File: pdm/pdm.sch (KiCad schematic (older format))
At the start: 30 parts, among them J1 Conn_01x04_Male, J2 Conn_01x04_Female, J3 Conn_01x02_Male, J4 Conn_01x12_Male, U1 SN65HVD233, U2 LM2937xS, Y1 32Mhz

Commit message: polished layout
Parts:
- gave numbers to parts that had none: 1
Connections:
- net act1: now also U3.13 (PA7); no longer U3.14 (PB0)
- net act2: now also U3.15 (PB1); no longer U3.26 (PB3)
- net act3: now also U3.19 (PA9); no longer U3.13 (PA7)
- net act4: now also U3.26 (PB3); no longer U3.20 (PA10)
- net act5: now also U3.27 (PB4); no longer U3.19 (PA9)
- net fuse1: now also U3.12 (PA6); no longer U3.25 (PA15)
- net fuse2: now also U3.14 (PB0); no longer U3.15 (PB1)
- net fuse3: now also U3.18 (PA8); no longer U3.12 (PA6)
- net fuse4: now also U3.25 (PA15); no longer U3.27 (PB4)
- net fuse5: now also U3.28 (PB5); no longer U3.18 (PA8)
- net sense1: now also U3.10 (PA4); no longer U3.9 (PA3)
- net sense2: now also U3.9 (PA3); no longer U3.10 (PA4)
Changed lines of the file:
@@
 	1    0    0    -1
 $EndComp
-Text Label 5150 5400 0    50   ~ 0
+Text Label 5100 5400 0    50   ~ 0
 OSC_P
-Text Label 5150 5300 0    50   ~ 0
+Text Label 5100 5300 0    50   ~ 0
 OSC_N
 Wire Wire Line
-	5750 5400 5150 5400
-Wire Wire Line
-	5750 5300 5150 5300
+	5750 5400 5100 5400
+Wire Wire Line
+	5750 5300 5100 5300
 Wire Wire Line
 	5150 4700 5750 4700
@@
 Wire Wire Line
 	5450 9050 5700 9050
-Text Label 5100 5900 0    50   ~ 0
+Text Label 7400 6200 2    50   ~ 0
 fuse4
 Wire Wire Line
-	6750 5700 7400 5700
-Text Label 7400 5700 2    50   ~ 0
+	5750 5800 5100 5800
+Text Label 5100 5800 0    50   ~ 0
 act4
 Wire Wire Line
-	5750 5900 5100 5900
+	6750 6200 7400 6200
 Wire Wire Line
 	6150 6450 6250 6450
@@
 	2800 1850 3100 1850
 Wire Wire Line
-	6750 6200 7400 6200
-Text Label 7400 6200 2    50   ~ 0
+	6750 5300 7400 5300
+Text Label 7400 5300 2    50   ~ 0
 fuse1
-Wire Wire Line
-	6750 5400 7400 5400
-Text Label 7400 5400 2    50   ~ 0
-act3
-Text Label 7400 5300 2    50   ~ 0
-fuse3
-Wire Wire Line
-	6750 5300 7400 5300
-Text Label 7400 5600 2    50   ~ 0
-act5
-Text Label 7400 5500 2    50   ~ 0
-fuse5
-Wire Wire Line
-	6750 5500 7400 5500
-Wire Wire Line
-	6750 5600 7400 5600
 $Comp
 L pdm-rescue:TestPoint_Probe-Connector TP?
@@
 Wire Wire Line
 	3200 7100 3200 7200
+Text Label 7400 5400 2    50   ~ 0
+act1
+Wire Wire Line
+	6750 5400 7400 5400
 Text Label 5100 5600 0    50   ~ 0
-act1
+fuse2
 Wire Wire Line
 	5750 5600 5100 5600
+Wire Wire Line
+	5750 5700 5100 5700
 Text Label 5100 5700 0    50   ~ 0
-fuse2
-Wire Wire Line
-	5750 5700 5100 5700
-Wire Wire Line
-	5750 5800 5100 5800
-Text Label 5100 5800 0    50   ~ 0
 act2
 $Comp
@@
 	2850 2050 2650 2050
 $Comp
-L MCU_ST_STM32L4:STM32L432KCUx U?
+L MCU_ST_STM32L4:STM32L432KCUx U3
 U 1 1 60CFF808
 P 6250 5400
-F 0 "U?" H 6250 6481 50  0000 C CNN
+F 0 "U3" H 6250 6481 50  0000 C CNN
 F 1 "STM32L432KCUx" H 6250 6390 50  0000 C CNN
 F 2 "Package_DFN_QFN:QFN-32-1EP_5x5mm_P0.5mm_EP3.45x3.45mm" H 5850 4500 50  0001 R CNN
@@
 Wire Wire Line
 	6750 4700 7400 4700
-Text Label 7400 5000 2    50   ~ 0
+Text Label 7400 5100 2    50   ~ 0
 sense1
 Wire Wire Line
-	6750 5000 7400 5000
+	6750 5100 7400 5100
 Wire Wire Line
 	6750 4900 7400 4900
 Text Label 7400 4900 2    50   ~ 0
 sense3
-Text Label 7400 5100 2    50   ~ 0
+Text Label 7400 5000 2    50   ~ 0
 sense2
 Wire Wire Line
-	6750 5100 7400 5100
+	6750 5000 7400 5000
 Text Label 7400 5200 2    50   ~ 0
 DAC2
@@
 Wire Wire Line
 	6350 4450 6350 4500
+Wire Wire Line
+	5750 5900 5100 5900
+Wire Wire Line
+	5750 6000 5100 6000
+Text Label 5100 6000 0    50   ~ 0
+fuse5
+Text Label 5100 5900 0    50   ~ 0
+act5
+Wire Wire Line
+	6750 5500 7400 5500
+Text Label 7400 5500 2    50   ~ 0
+fuse3
+Text Label 7400 5600 2    50   ~ 0
+act3
+Wire Wire Line
+	6750 5600 7400 5600
 $EndSCHEMATC

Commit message: general changes
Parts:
- removed J2: Conn_01x04_Female, Connector_PinHeader_2.54mm:PinHeader_1x04_P2.54mm_Vertical, symbol Connector:Conn_01x04_Female
- added H5: MountingHole, pdm_v2:pepe-v2, symbol Mechanical:MountingHole
- added H6: MountingHole, pdm_v2:uwam-logo, symbol Mechanical:MountingHole
- added H7: MountingHole, pdm_v2:checklist, symbol Mechanical:MountingHole
- added H8: MountingHole, pdm_v2:meme-qr, symbol Mechanical:MountingHole
- added J2: Conn_01x14_Female, Connector_PinSocket_1.27mm:PinSocket_2x07_P1.27mm_Vertical_SMD, symbol Connector:Conn_01x14_Female
- C10: value 1uF -> 0.1pF; Digi-Key_PN 1276-1859-2-ND -> (none)
- U3: footprint Package_DFN_QFN:QFN-32-1EP_5x5mm_P0.5mm_EP3.45x3.45mm -> Package_DFN_QFN:QFN-32-1EP_5x5mm_P0.5mm_EP3.45x3.45mm_ThermalVias
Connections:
- net +3V3: now also J2.3 (Pin_3); no longer C10.1
- net GND: now also J2.5 (Pin_5), J2.7 (Pin_7)
- net NRST: now also C10.1, J2.12 (Pin_12)
- net SWCLK: now also J2.6 (Pin_6)
- net SWDIO: now also J2.4 (Pin_4)
- new net GNDDetect: J2.11 (Pin_11)
- new net JCLK: J2.9 (Pin_9)
- new net SWO: J2.8 (Pin_8)
- new net T_JTDI: J2.10 (Pin_10)
- new net VCP_RX: J2.13 (Pin_13)
- new net VCP_TX: J2.14 (Pin_14)
- no-connect marks 0 -> 11

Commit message: Initial commit
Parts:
- removed J2: Conn_01x14_Female, Connector_PinSocket_1.27mm:PinSocket_2x07_P1.27mm_Vertical_SMD, symbol Connector:Conn_01x14_Female
- added TP20: TestPoint_Probe, TestPoint:TestPoint_THTPad_1.0x1.0mm_Drill0.5mm, symbol pdm-rescue:TestPoint_Probe-Connector
- added U9: STLINK_V3, pdm_v2:STM32_Programmer, symbol Project_Libraries:STLINK_V3
- C1, C4, C6, C7: Mouser PN 603-CC0805MRX77BB104 -> 80-C0603C104K3RC7013
- C10: Mouser PN (none) -> 791-RF18N0R1B500CT
- C2, C3: Mouser PN 603-CC805JRNPO9BN160 -> C0603C160J3HACTU
- C5: Mouser PN 603-CC0805MKX58BB105 -> 80-C0603C160J3HACTU
- C8: Mouser PN 603-CC0805KFX5R8BB47 -> 80-C0603C104K3RC7013
- C9: footprint Capacitor_SMD:C_0603_1608Metric -> Capacitor_SMD:C_0805_2012Metric_Pad1.18x1.45mm_HandSolder; Mouser PN (none) -> 81-GRM21BR61E106MA3L
- D1: Mouser PN 630-HSMA-C170-T0000 -> 710-150060AS75000
- R1: Mouser PN 279-CPF-A-0805B120RE -> 755-ESR03EZPF1200
- R2: Mouser PN 603-RC0805JR-07120RL -> 755-ESR03EZPF1200
- TP1, TP2: footprint TestPoint:TestPoint_Pad_D1.0mm -> TestPoint:TestPoint_THTPad_1.0x1.0mm_Drill0.5mm
- U3: footprint Package_DFN_QFN:QFN-32-1EP_5x5mm_P0.5mm_EP3.45x3.45mm_ThermalVias -> Package_DFN_QFN:QFN-32-1EP_5x5mm_P0.5mm_EP3.45x3.45mm; Mouser PN (none) -> 511-STM32L432KCU6
- Y1: Mouser PN (none) -> 559-280LF-080
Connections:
- net +3V3: now also U9.3 (T_VCC)
- net GND: now also U3.31 (PH3), TP20.1, U9.11 (GND_DETECT), U9.5 (GND), U9.7 (GND)
- net NRST: now also U9.12 (NRST)
- net SWCLK: now also U9.6 (SWCLK)
- net SWDIO: now also U9.4 (SWDIO)
- net _N: now also CANH_TP1.1, J3.1 (Pin_1), R1.2, U1.6 (CANL); no longer CANL_Test1.1, J3.2 (Pin_2), R1.1, U1.7 (CANH)
- net _P: now also CANL_Test1.1, J3.2 (Pin_2), R1.1, U1.7 (CANH); no longer CANH_TP1.1, J3.1 (Pin_1), R1.2, U1.6 (CANL)
- no-connect marks 11 -> 8
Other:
- moved on the sheet: C10, U3

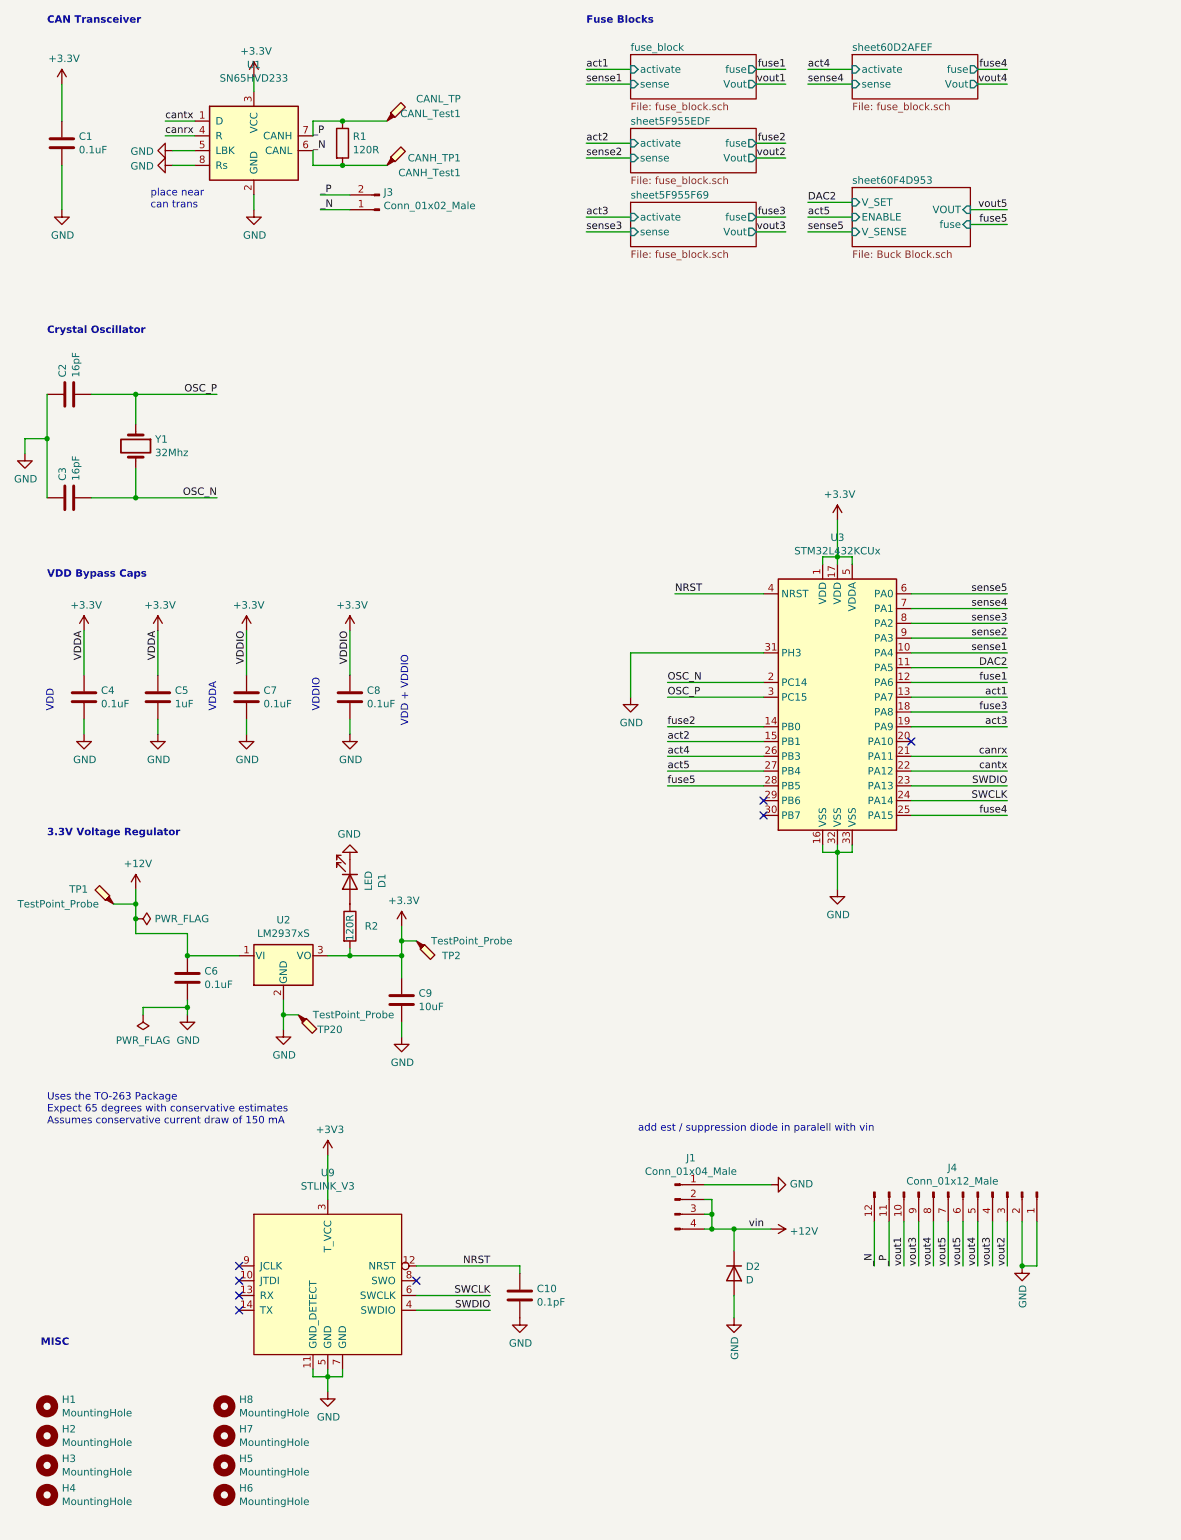
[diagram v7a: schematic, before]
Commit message: changed parts layout
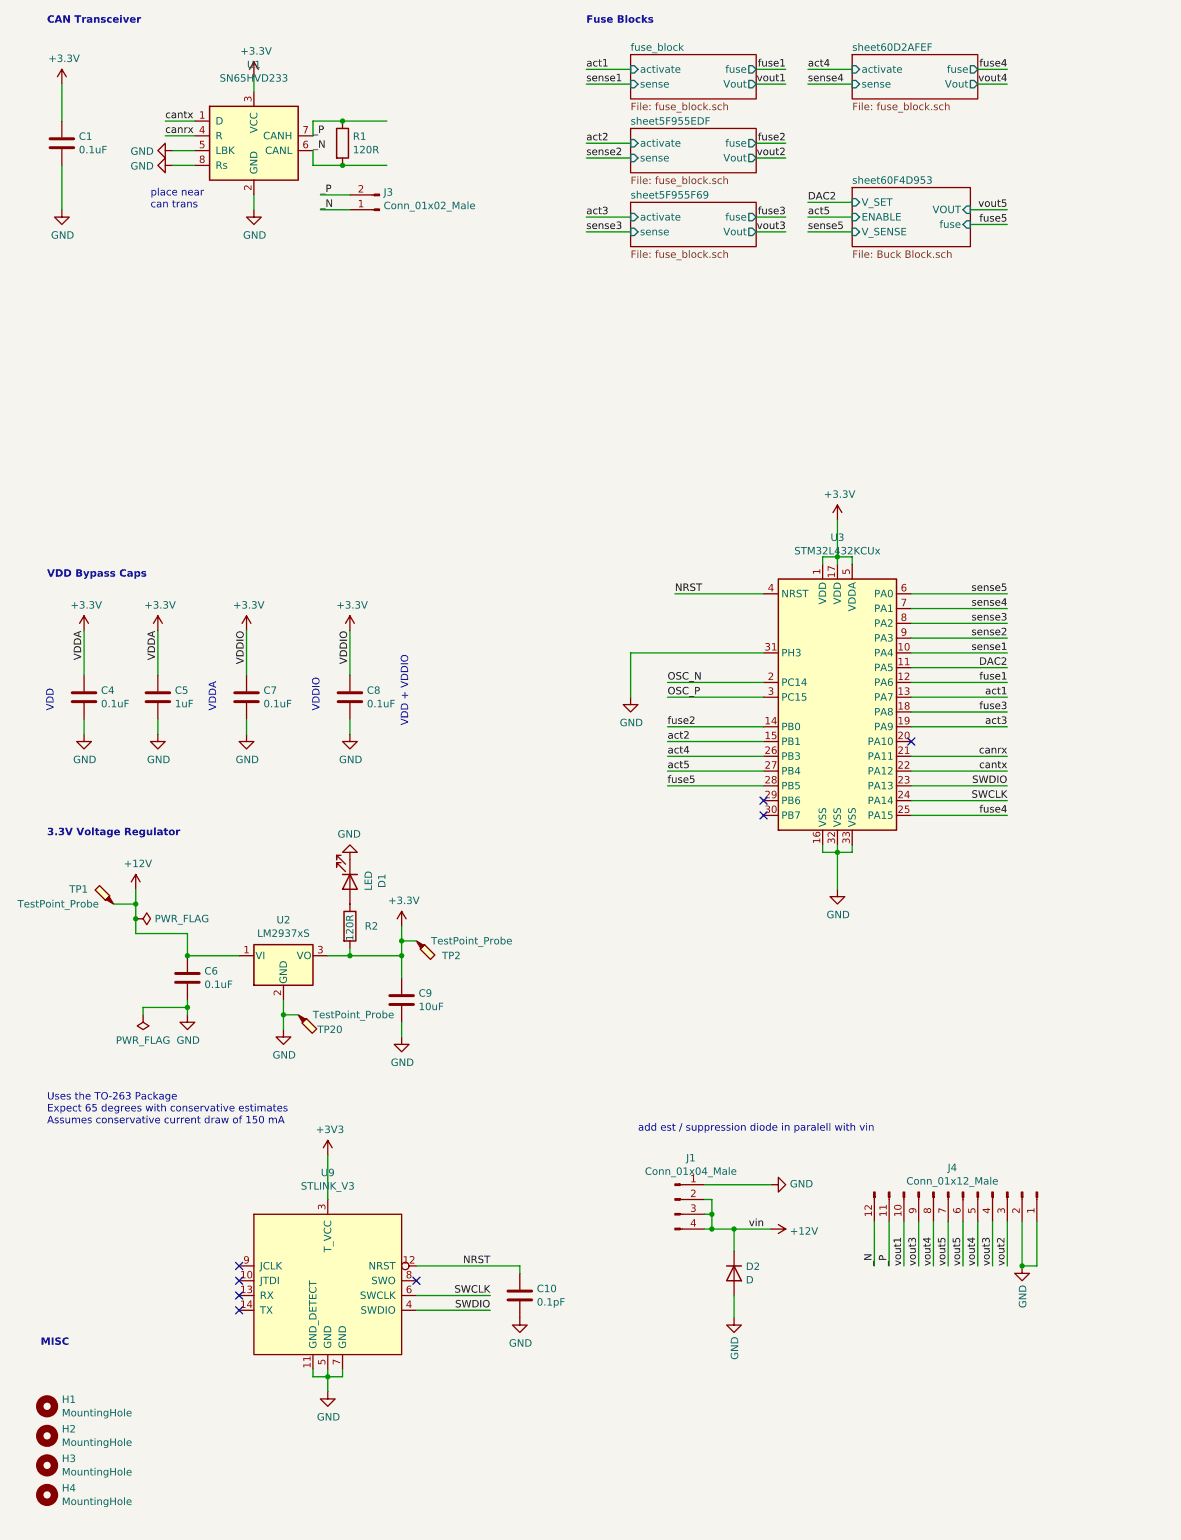
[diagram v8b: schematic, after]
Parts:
- removed C2, C3: 16pF, Capacitor_SMD:C_0603_1608Metric, symbol pdm-rescue:C-Device
- removed CANH_TP1: CANH_Test1, TestPoint:TestPoint_Pad_D1.0mm, symbol pdm-rescue:TestPoint_Probe-Connector
- removed CANL_Test1: CANL_TP, TestPoint:TestPoint_Pad_D1.0mm, symbol pdm-rescue:TestPoint_Probe-Connector
- removed H5: MountingHole, pdm_v2:pepe-v2, symbol Mechanical:MountingHole
- removed H6: MountingHole, pdm_v2:uwam-logo, symbol Mechanical:MountingHole
- removed H7: MountingHole, pdm_v2:checklist, symbol Mechanical:MountingHole
- removed H8: MountingHole, pdm_v2:meme-qr, symbol Mechanical:MountingHole
- removed Y1: 32Mhz, Crystal:Crystal_SMD_HC49-SD, symbol Device:Crystal
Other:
- note removed: "Crystal Oscillator"
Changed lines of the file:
@@
 Wire Wire Line
 	2600 1850 2600 1750
-Wire Wire Line
-	1100 4100 1400 4100
-Wire Wire Line
-	1400 4100 1400 3900
-Connection ~ 1400 4100
-Wire Wire Line
-	1400 3600 1400 3400
-Connection ~ 1400 3400
-Wire Wire Line
-	1400 3400 1100 3400
 $Comp
 L pdm-rescue:+3.3V-power #PWR022
@@
 Text Notes 800  900  0    50   ~ 10
 CAN Transceiver
-Text Notes 800  3000 0    50   ~ 10
-Crystal Oscillator
 Text Notes 800  4650 0    50   ~ 10
 VDD Bypass Caps
@@
 Text Label 1600 1650 0    50   ~ 0
 canrx
-Text Label 1950 3400 2    50   ~ 0
-OSC_P
-Wire Wire Line
-	800  3400 800  3700
-Text Label 1950 4100 2    50   ~ 0
-OSC_N
 Text Label 4450 1200 0    50   ~ 0
 act1
@@
 vout2
 Wire Wire Line
-	1400 3400 1950 3400
-Wire Wire Line
-	1400 4100 1950 4100
-Wire Wire Line
 	6700 9000 6700 9300
 Text Label 6700 9300 1    50   ~ 0
@@
 Wire Wire Line
 	1750 7550 1750 7600
-$Comp
-L power:GND #PWR0101
-U 1 1 60D729C1
-P 650 3800
-F 0 "#PWR0101" H 650 3550 50  0001 C CNN
-F 1 "GND" H 655 3627 50  0000 C CNN
-F 2 "" H 650 3800 50  0001 C CNN
-F 3 "" H 650 3800 50  0001 C CNN
-	1    650  3800
-	1    0    0    -1
-$EndComp
-Wire Wire Line
-	650  3800 650  3700
-Wire Wire Line
-	650  3700 800  3700
-Connection ~ 800  3700
-Wire Wire Line
-	800  3700 800  4100
 Wire Wire Line
 	2800 1550 3100 1550
@@
 $EndComp
 $Comp
-L pdm-rescue:TestPoint_Probe-Connector CANH_TP?
-U 1 1 6002DB6D
-P 3100 1850
-AR Path="/5F955F6E/6002DB6D" Ref="CANH_TP?"  Part="1"
-AR Path="/5F955EE4/6002DB6D" Ref="CANH_TP?"  Part="1"
-AR Path="/5F94FFF3/6002DB6D" Ref="CANH_TP?"  Part="1"
-AR Path="/5F956034/6002DB6D" Ref="CANH_TP?"  Part="1"
-AR Path="/5F9560D2/6002DB6D" Ref="CANH_TP?"  Part="1"
-AR Path="/6002DB6D" Ref="CANH_TP1"  Part="1"
-F 0 "CANH_TP1" V 3150 2350 50  0000 R CNN
-F 1 "CANH_Test1" V 3050 2350 50  0000 R CNN
-F 2 "TestPoint:TestPoint_Pad_D1.0mm" H 3300 1850 50  0001 C CNN
-F 3 "~" H 3300 1850 50  0001 C CNN
-	1    3100 1850
-	0    1    -1   0
-$EndComp
-$Comp
-L pdm-rescue:TestPoint_Probe-Connector CANL_Test?
-U 1 1 6002ED89
-P 3100 1550
-AR Path="/5F955F6E/6002ED89" Ref="CANL_Test?"  Part="1"
-AR Path="/5F955EE4/6002ED89" Ref="CANL_Test?"  Part="1"
-AR Path="/5F94FFF3/6002ED89" Ref="CANL_Test?"  Part="1"
-AR Path="/5F956034/6002ED89" Ref="CANL_Test?"  Part="1"
-AR Path="/5F9560D2/6002ED89" Ref="CANL_Test?"  Part="1"
-AR Path="/6002ED89" Ref="CANL_Test1"  Part="1"
-F 0 "CANL_Test1" V 3150 2050 50  0000 R CNN
-F 1 "CANL_TP" V 3250 2050 50  0000 R CNN
-F 2 "TestPoint:TestPoint_Pad_D1.0mm" H 3300 1550 50  0001 C CNN
-F 3 "~" H 3300 1550 50  0001 C CNN
-	1    3100 1550
-	0    1    -1   0
-$EndComp
-$Comp
-L Device:Crystal Y1
-U 1 1 60D44625
-P 1400 3750
-F 0 "Y1" V 1354 3881 50  0000 L CNN
-F 1 "32Mhz" V 1445 3881 50  0000 L CNN
-F 2 "Crystal:Crystal_SMD_HC49-SD" H 1400 3750 50  0001 C CNN
-F 3 "https://www.foxonline.com/wp-content/uploads/pdfs/C4SD.pdf" H 1400 3750 50  0001 C CNN
-F 4 "631-1010-2-ND" H 1400 3750 50  0001 C CNN "Digi-Key_PN"
-F 5 "559-280LF-080" H 1400 3750 50  0001 C CNN "Mouser PN"
-	1    1400 3750
-	0    1    1    0
-$EndComp
-$Comp
 L Device:C C9
 U 1 1 6102CE14
@@
 	1    0    0    -1
 $EndComp
-$Comp
-L pdm-rescue:C-Device C3
-U 1 1 5F9D7172
-P 950 4100
-F 0 "C3" H 1065 4146 50  0000 L CNN
-F 1 "16pF" H 1065 4055 50  0000 L CNN
-F 2 "Capacitor_SMD:C_0603_1608Metric" H 988 3950 50  0001 C CNN
-F 3 "~" H 950 4100 50  0001 C CNN
-F 4 "478-10292-2-ND" H 950 4100 50  0001 C CNN "Digi-Key_PN"
-F 5 "C0603C160J3HACTU" H 950 4100 50  0001 C CNN "Mouser PN"
-	1    950  4100
-	0    -1   -1   0
-$EndComp
-$Comp
-L pdm-rescue:C-Device C2
-U 1 1 5F9D5FE7
-P 950 3400
-F 0 "C2" H 1065 3446 50  0000 L CNN
-F 1 "16pF" H 1065 3355 50  0000 L CNN
-F 2 "Capacitor_SMD:C_0603_1608Metric" H 988 3250 50  0001 C CNN
-F 3 "~" H 950 3400 50  0001 C CNN
-F 4 "478-10292-2-ND" H 950 3400 50  0001 C CNN "Digi-Key_PN"
-F 5 "C0603C160J3HACTU" H 950 3400 50  0001 C CNN "Mouser PN"
-	1    950  3400
-	0    -1   -1   0
-$EndComp
 Wire Wire Line
 	3300 9600 3800 9600
@@
 	1    0    0    -1
 $EndComp
-$Comp
-L Mechanical:MountingHole H6
-U 1 1 60E0481B
-P 2000 10850
-F 0 "H6" H 2100 10896 50  0000 L CNN
-F 1 "MountingHole" H 2100 10805 50  0000 L CNN
-F 2 "pdm_v2:uwam-logo" H 2000 10850 50  0001 C CNN
-F 3 "~" H 2000 10850 50  0001 C CNN
-	1    2000 10850
-	1    0    0    -1
-$EndComp
-$Comp
-L Mechanical:MountingHole H5
-U 1 1 60E053CE
-P 2000 10650
-F 0 "H5" H 2100 10696 50  0000 L CNN
-F 1 "MountingHole" H 2100 10605 50  0000 L CNN
-F 2 "pdm_v2:pepe-v2" H 2000 10650 50  0001 C CNN
-F 3 "~" H 2000 10650 50  0001 C CNN
-	1    2000 10650
-	1    0    0    -1
-$EndComp
-$Comp
-L Mechanical:MountingHole H7
-U 1 1 60E0BB85
-P 2000 10450
-F 0 "H7" H 2100 10496 50  0000 L CNN
-F 1 "MountingHole" H 2100 10405 50  0000 L CNN
-F 2 "pdm_v2:checklist" H 2000 10450 50  0001 C CNN
-F 3 "~" H 2000 10450 50  0001 C CNN
-	1    2000 10450
-	1    0    0    -1
-$EndComp
-$Comp
-L Mechanical:MountingHole H8
-U 1 1 60FCFB00
-P 2000 10250
-F 0 "H8" H 2100 10296 50  0000 L CNN
-F 1 "MountingHole" H 2100 10205 50  0000 L CNN
-F 2 "pdm_v2:meme-qr" H 2000 10250 50  0001 C CNN
-F 3 "~" H 2000 10250 50  0001 C CNN
-	1    2000 10250
-	1    0    0    -1
-$EndComp
